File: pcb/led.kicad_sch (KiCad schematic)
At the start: 328 parts, among them U1 IS31FL3729, U2 IS31FL3729, U3 IS31FL3729, U4 IS31FL3729

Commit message: v2
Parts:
- removed R13, R15: 10k, Resistor_SMD:R_0603_1608Metric, symbol Device:R
- removed U1, U2, U3, U4: IS31FL3729, misc:eTQFP-32_7x7mm_P0.8mm, symbol ic:IS31FL3729
- added C12, C17, C18, C7: 1uF, Capacitor_SMD:C_0603_1608Metric, symbol Device:C_Small
- added C13, C14, C5, C6: 0.1uF, Capacitor_SMD:C_0603_1608Metric, symbol Device:C_Small
- added U1, U2: IS31FL3741, ic:QFN-60-1EP_7x7mm_P0.4mm_EP5.4x5.4mm_ThermalVias, symbol ic:IS31FL3741
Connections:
- net GND: now also C12.2, C13.2, C14.2, C17.2, C18.2, C5.2, C6.2, C7.2, U1.12 (GND), U1.36 (GND), U1.55 (GND), U1.61 (GND), U1.8 (ADDR), U2.12 (GND), U2.36 (GND), U2.55 (GND), U2.61 (GND)
- net RGB_B0: now also U2.41 (CS15)
- net RGB_B1: now also U2.38 (CS12)
- net RGB_B2: now also U2.34 (CS9)
- net RGB_B3: now also U2.31 (CS6)
- net RGB_B4: now also U2.4 (CS37)
- net RGB_B5: now also U2.1 (CS34)
- net RGB_B6: now also U2.58 (CS31)
- net RGB_B7: now also U2.54 (CS28)
- net RGB_C0: now also U2.23 (SW8)
- net RGB_C1: now also U2.22 (SW7)
- net RGB_C2: now also U2.21 (SW6)
- net RGB_C3: now also U2.20 (SW5)
- net RGB_C4: now also U2.19 (SW4)
- net RGB_C5: now also U2.18 (SW3)
- net RGB_C6: now also U2.17 (SW2)
- net RGB_C7: now also U2.16 (SW1)
- net RGB_G0: now also U2.42 (CS16)
- net RGB_G1: now also U2.39 (CS13)
- net RGB_G2: now also U2.35 (CS10)
- net RGB_G3: now also U2.32 (CS7)
- net RGB_G4: now also U2.5 (CS38)
- net RGB_G5: now also U2.2 (CS35)
- net RGB_G6: now also U2.59 (CS32)
- net RGB_G7: now also U2.56 (CS29)
- net RGB_R0: now also U2.43 (CS17)
- net RGB_R1: now also U2.40 (CS14)
- net RGB_R2: now also U2.37 (CS11)
- net RGB_R3: now also U2.33 (CS8)
- net RGB_R4: now also U2.6 (CS39)
- net RGB_R5: now also U2.3 (CS36)
- net RGB_R6: now also U2.60 (CS33)
- net RGB_R7: now also U2.57 (CS30)
- net SCL: now also U1.10 (SCL), U2.10 (SCL)
- net SDA: now also U1.9 (SDA), U2.9 (SDA)
- net W_C00: now also U1.42 (CS16)
- net W_C01: now also U1.41 (CS15)
- net W_C02: now also U1.40 (CS14)
- net W_C03: now also U1.39 (CS13)
- net W_C04: now also U1.38 (CS12)
- net W_C05: now also U1.37 (CS11)
- net W_C06: now also U1.35 (CS10)
- net W_C07: now also U1.34 (CS9)
- net W_C08: now also U1.33 (CS8)
- net W_C09: now also U1.32 (CS7)
- net W_C10: now also U1.31 (CS6)
- net W_C11: now also U1.30 (CS5)
- net W_C12: now also U1.29 (CS4)
- net W_C13: now also U1.28 (CS3)
- net W_C14: now also U1.27 (CS2)
- net W_C15: now also U1.26 (CS1)
- net W_C16: now also U1.6 (CS39)
- net W_C17: now also U1.5 (CS38)
- net W_C18: now also U1.4 (CS37)
- net W_C19: now also U1.3 (CS36)
- net W_C20: now also U1.2 (CS35)
- net W_C21: now also U1.1 (CS34)
- net W_C22: now also U1.60 (CS33)
- net W_C23: now also U1.59 (CS32)
- net W_C24: now also U1.58 (CS31)
- net W_C25: now also U1.57 (CS30)
- net W_C26: now also U1.56 (CS29)
- net W_C27: now also U1.54 (CS28)
- net W_C28: now also U1.53 (CS27)
- net W_C29: now also U1.52 (CS26)
- net W_C30: now also U1.51 (CS25)
- net W_C31: now also U1.50 (CS24)
- net W_R0: now also U1.16 (SW1)
- net W_R1: now also U1.17 (SW2)
- net W_R2: now also U1.18 (SW3)
- net W_R3: now also U1.19 (SW4)
- net W_R4: now also U1.20 (SW5)
- net W_R5: now also U1.21 (SW6)
- net W_R6: now also U1.22 (SW7)
- net W_R7: now also U1.23 (SW8)
- net ~{SHDN}: now also U1.11 (~{SDB}), U2.11 (~{SDB})
- net at R16.2: now also U2.13 (R_EXT)
- net at R14.2: now also U1.13 (R_EXT)
- new net PVCC: C12.1, C13.1, C14.1, C17.1, C18.1, C5.1, C6.1, C7.1, U1.14 (AVCC), U1.15 (PVCC), U1.25 (PVCC), U2.14 (AVCC), U2.15 (PVCC), U2.25 (PVCC), U2.8 (ADDR)
- no-connect marks 8 -> 0
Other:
- moved on the sheet: R14, R16

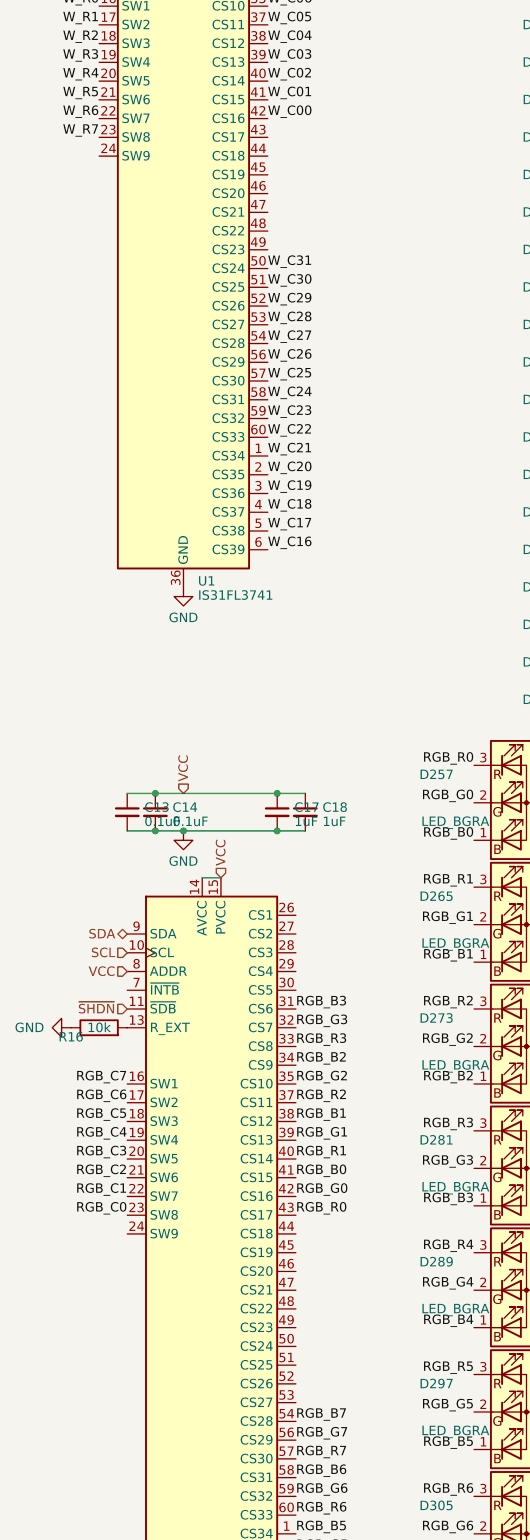
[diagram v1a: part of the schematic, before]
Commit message: stamp ground vias; ERC
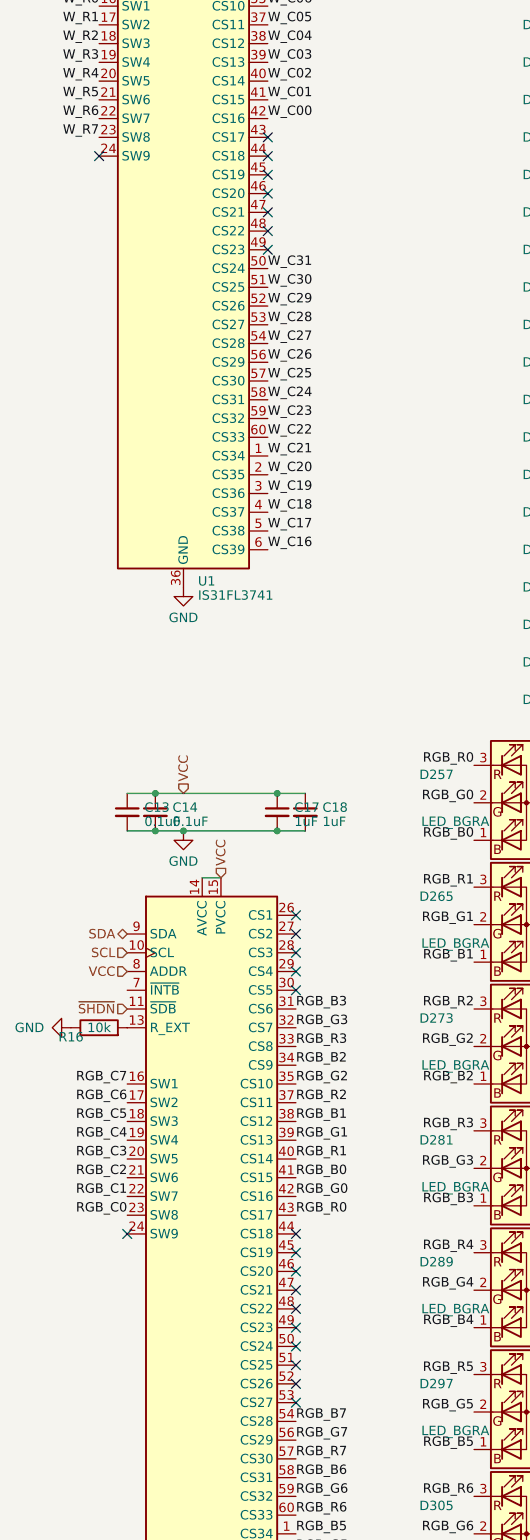
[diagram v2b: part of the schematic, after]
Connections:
- no-connect marks 0 -> 24
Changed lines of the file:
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@@
   (junction (at 95.25 -34.29) (diameter 0) (color 0 0 0 0)
   )
+  (no_connect (at 114.3 181.61))
+  (no_connect (at 110.49 27.94))
+  (no_connect (at 110.49 20.32))
+  (no_connect (at 114.3 186.69))
+  (no_connect (at 114.3 184.15))
+  (no_connect (at 110.49 33.02))
+  (no_connect (at 114.3 179.07))
+  (no_connect (at 114.3 166.37))
+  (no_connect (at 110.49 17.78))
+  (no_connect (at 114.3 168.91))
+  (no_connect (at 114.3 173.99))
+  (no_connect (at 114.3 176.53))
+  (no_connect (at 91.44 166.37))
+  (no_connect (at 114.3 128.27))
+  (no_connect (at 114.3 130.81))
+  (no_connect (at 87.63 20.32))
+  (no_connect (at 114.3 171.45))
+  (no_connect (at 114.3 133.35))
+  (no_connect (at 110.49 22.86))
+  (no_connect (at 114.3 125.73))
+  (no_connect (at 110.49 30.48))
+  (no_connect (at 114.3 123.19))
+  (no_connect (at 114.3 189.23))
+  (no_connect (at 110.49 25.4))
   (wire (pts (xy 256.54 -12.7) (xy 256.54 -7.62))
     (stroke (width 0) (type default))
@@
       (effects (font (size 1.27 1.27)) hide)
     )
-    (property "Datasheet" "https://www.lumissil.com/assets/pdf/core/IS31FL3729_DS.pdf" (at 59.69 187.96 0)
+    (property "Datasheet" "https://www.mouser.com/datasheet/2/198/IS31FL3741A_DS-1839558.pdf" (at 59.69 187.96 0)
       (effects (font (size 1.27 1.27)) hide)
     )
@@
       (effects (font (size 1.27 1.27)) hide)
     )
-    (property "Datasheet" "https://www.lumissil.com/assets/pdf/core/IS31FL3729_DS.pdf" (at 55.88 41.91 0)
+    (property "Datasheet" "https://www.mouser.com/datasheet/2/198/IS31FL3741A_DS-1839558.pdf" (at 55.88 41.91 0)
       (effects (font (size 1.27 1.27)) hide)
     )
